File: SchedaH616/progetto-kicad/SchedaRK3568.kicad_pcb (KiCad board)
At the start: 6 copper layers, 50 x 70 mm, 443 parts, among them J1 BUS_POWER_MIKILAB, J103 DC-005-5A-2.0, J104 TYPE-C-31-M-12, J2 BUS_MIKILAB_MAIN, J301 UART2 debug, J401 DM3AT-SF-PEJM5, J501 HR911130C, J601 U.FL, J701 SMA antenna, J702 SMA PPS OUT, J703 SMA STROBE IN, J704 PPS/STROBE, J801 TYPE-C-31-M-12, SW301 RESET, SW302 RECOVERY, U101 TPS56637RPAR, U103 TPS2121RUXR, U104 FUSB302BMPX, U105 SY6280AAC, U107 TPD2EUSB30ADRTR, U108 TPS2121RUXR, U201 RK809-5, U202 TCS4525_WT, U203 TPS563201DDCR, U204 AP2112K-1.8TRG1, U205 AP2112K-2.5TRG1, U301 RK3568, U302 TPD4E05U06DQA, U303 TPD4E05U06DQA, U304 TPD4E05U06DQA, U305 TPD4E05U06DQA, U306 TPD4E05U06DQA, U307 TPD4E05U06DQA, U401 K4AAG165WA-BCWE, U402 FEMDNN064G-C9A61, U403 TPD4E05U06DQA, U404 TPD4E05U06DQA, U501 RTL8211F-CG, U502 25AA02E48T-I/OT, U601 AP6256, U701 NEO-M9N-00B, U702 74LVC1G17, U703 74LVC1G17, U801 TPS2553DBVR, U802 USBLC6-2SC6, Y201 32.768kHz, Y301 24MHz, Y501 25MHz

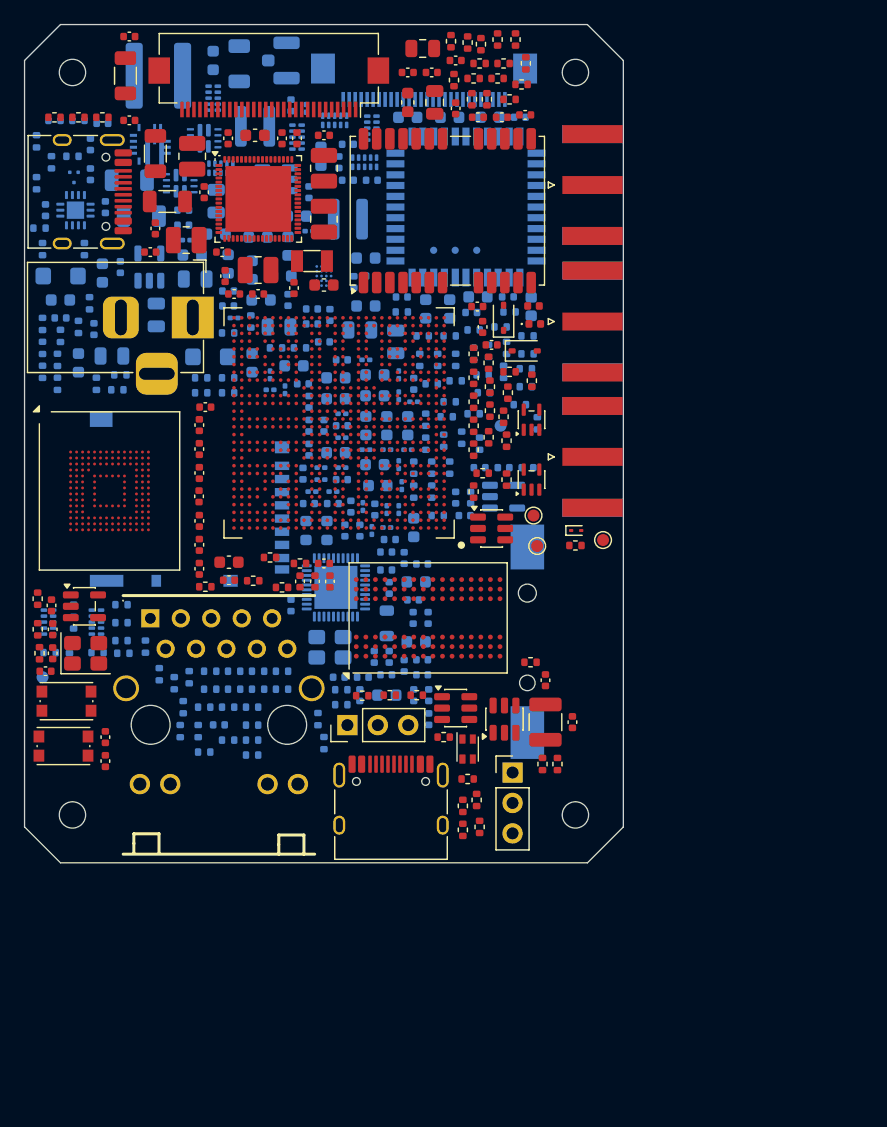
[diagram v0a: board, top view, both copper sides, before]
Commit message: SchedaH616: componenti specifici dalla libreria MIKILAB
- simbolo e footprint MIKILAB per RK809-5, TCS4525, K4AAG165WA-BCWE, FEMDNN064G-C9A61,
  AP2112K-1.8TRG1, TPS56637RPAR, TPS2121RUXR, SY6280AAC, TPS563201DDCR, TPS2553DBVR,
  TYPE-C-31-M-12, FH12-30S-0.5SH, FPC-05F-28PH20, HR911130C, 25AA02E48T-I/OT, DM3AT-SF-PEJM5;
  simbolo MIKILAB per l'AP6256
- restano nella libreria di progetto: RK3568 (pad EasyEDA da 0.35 mm, niente fanout 5/5 mil),
  simbolo RTL8211F (quello MIKILAB ha pin di alimentazione nascosti), footprint AP6256 LGA-47,
  portapila BS-12; motivazioni in docs/scelte-progetto.md
- kilib.mik() carica simboli e footprint dalla libreria (variabile MIKILAB); matrice ERC:
  pin unspecified dei simboli EasyEDA OK
- netlist identica a 4ca35fc (439 componenti, 314 net); ERC 0, parita' 0, DRC 0 (solo
  collegamenti da fare); footprint corretti nella libreria MIKILAB 8b990c4

Co-Authored-By: Claude Opus 5.5 (1M context) <noreply@anthropic.com>
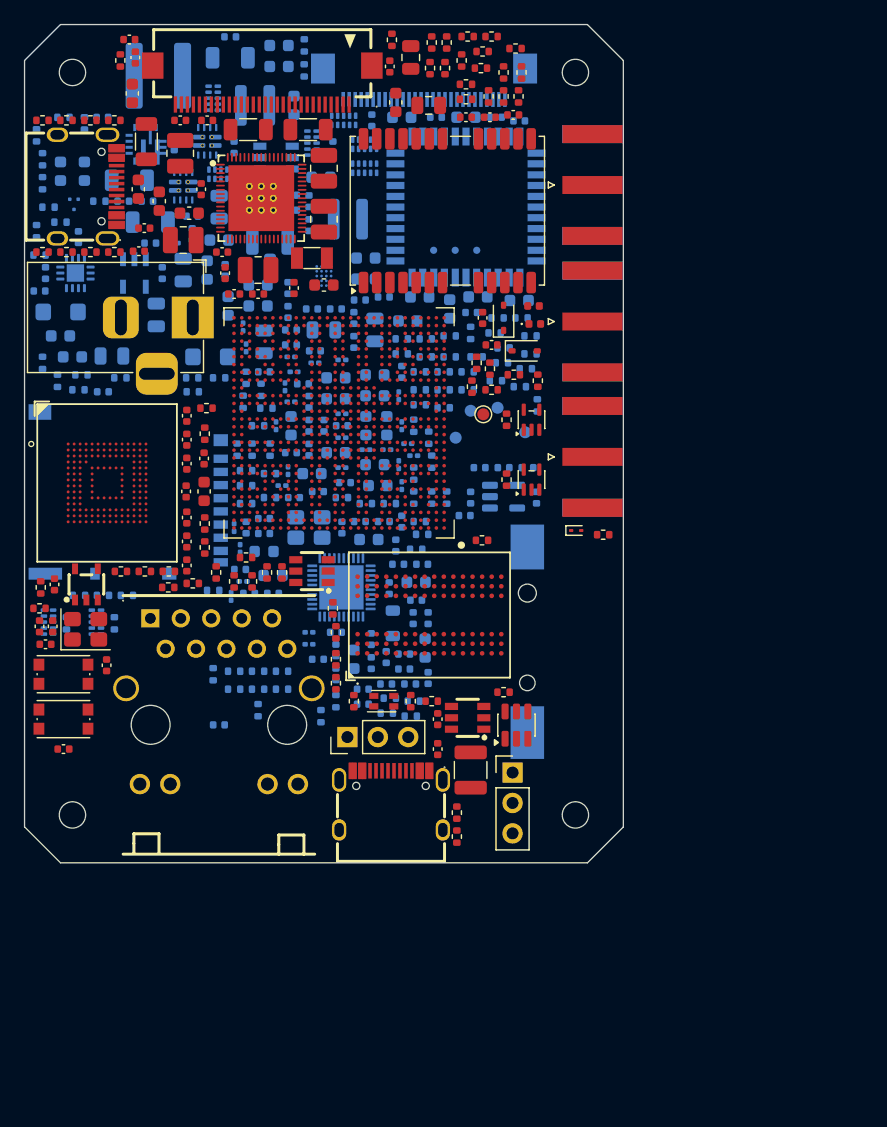
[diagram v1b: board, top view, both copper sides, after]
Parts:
- C104, C133, C203, C208, C210, C217, C228, C260, C339, C341, C425, C511, C512, C513, C515, C607, C702, R315, R319, R329, R331, R339, R402, R418, R420, R421, R516, R601, R603, R604, R609, R806, R807, TP202, TP702: moved to B.Cu
- C127, C134, C206, C209, C212, C213, C220, C233, C239, R107, R108, R110, R111, R114, R115, R202, R203, R309, R333, R336, R407, R409, R410, R412, R503, R507, R509, R511, R519, R526, R602, R605, R608: moved to F.Cu
- J1: footprint Connector_FFC-FPC:Hirose_FH12-30S-0.5SH_1x30-1MP_P0.50mm_Horizontal -> MIKILAB_FH12_30S_0_5SH:FPC-SMD_FH12-30S-0.5SH-55
- J104, J801: footprint Connector_USB:USB_C_Receptacle_HRO_TYPE-C-31-M-12 -> MIKILAB_TYPE_C_31_M_12:USB-C_SMD-TYPE-C-31-M-12_1
- J2: footprint Scheda:FPC-05F-28PH20 -> MIKILAB_FPC_05F_28PH20:FPC-SMD_28P-P0.50_FPC-05F-28PH20
- J401: footprint Connector_Card:microSD_HC_Hirose_DM3AT-SF-PEJM5 -> MIKILAB_DM3AT_SF_PEJM5:SD-SMD_DM3AT-SF-PEJM5
- J501: footprint Scheda:RJ45-TH_HR911130C -> MIKILAB_HR911130C:RJ45-TH_HR911130C
- U101: footprint Scheda:Texas_RPA0010A_VQFN-HR-10_3x3mm -> MIKILAB_TPS56637RPAR:VQFN-HR-10_L3.0-W3.0_RPA
- U103, U108: footprint Package_DFN_QFN:Texas_VQFN-HR-12_2x2.5mm_P0.5mm -> MIKILAB_TPS2121RUXR:IC_TPS2121RUXR
- U105: footprint Package_TO_SOT_SMD:SOT-23-5 -> MIKILAB_SY6280AAC:SOT-23-5_L3.0-W1.7-P0.95-LS2.8-BL
- U201: footprint Package_DFN_QFN:ArtInChip_QFN-68-1EP_7x7mm_P0.35mm_EP5.49x5.49mm -> MIKILAB_RK809_5:QFN-68_L7.0-W7.0-P0.35-BL-EP5.5
- U202: footprint Package_CSP:DiodesInc_GEA20_WLCSP-20_1.7x2.1mm_Layout4x5_P0.4mm -> MIKILAB_TCS4525:TCS4525_WLCSP-20_1.6x2.0mm_P0.4mm
- U203: footprint Package_TO_SOT_SMD:SOT-23-6 -> MIKILAB_TPS563201DDCR:TPS563201DDCR_SOT-23-6_L2.9-W1.6-P0.95-LS2.8-BR
- U204: footprint Package_TO_SOT_SMD:SOT-23-5 -> MIKILAB_AP2112K_1_8TRG1:SOT-25_L3.0-W1.6-P0.95-LS2.8-BL
- U401: footprint Package_BGA:BGA-96_9.0x13.0mm_Layout2x3x16_P0.8mm -> MIKILAB_K4AAG165WA_BCWE:BGA-96_L13.3-W10.3-P0.80_K4AAG165WA-BCWE
- U402: footprint Package_BGA:LFBGA-153_11.5x13mm_Layout14x14_P0.5mm -> MIKILAB_FEMDNN064G_C9A61:BGA-153_L13.0-W11.5-P0.50-TL_FORESEE_FEMDME
- U501: footprint Package_DFN_QFN:QFN-40-1EP_5x5mm_P0.4mm_EP3.6x3.6mm -> MIKILAB_RTL8211F_CG:QFN40P500X500X90-41N
- U502: footprint Package_TO_SOT_SMD:SOT-23-6 -> MIKILAB_25AA02E48T_I_OT:SOT-23-6_L2.9-W1.6-P0.95-LS2.8-BR
- U801: footprint Package_TO_SOT_SMD:SOT-23-6 -> MIKILAB_TPS2553DBVR:TPS2553DBVR_SOT-23-6_L2.9-W1.6-P0.95-LS2.8-BR
- moved TP101 42.1 mm to (137.3, 132.3)
- moved R203 34.5 mm to (135.2, 101.5), turned to 90 degrees
- moved R121 33.9 mm to (101.0, 109.2), turned to 90 degrees
- moved R115 33.5 mm to (130.7, 101.3)
- moved R122 33.4 mm to (101.0, 117.2), turned to 90 degrees
- moved R317 33.4 mm to (104.5, 130.5)
- moved R202 32.8 mm to (134.0, 101.5), turned to 90 degrees
- moved R604 32.4 mm to (123.4, 101.7)
- moved R128 32.0 mm to (133.5, 127.8), turned to 0 degrees
- moved C607 30.5 mm to (120.0, 129.0)
- moved R527 29.4 mm to (135.2, 139.5), turned to 90 degrees
- moved R313 27.5 mm to (108.0, 129.5), turned to 0 degrees
- moved R521 27.2 mm to (116.0, 145.8), turned to 90 degrees
- moved R516 25.9 mm to (117.5, 155.5), turned to 0 degrees
- moved C339 25.6 mm to (122.2, 126.8)
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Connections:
- U402 pad A1: (no net) -> unconnected-(U402B-NC-PadA1)
- U402 pad A10: (no net) -> unconnected-(U402B-NC-PadA10)
- U402 pad A11: (no net) -> unconnected-(U402B-NC-PadA11)
- U402 pad A12: (no net) -> unconnected-(U402B-NC-PadA12)
- U402 pad A13: (no net) -> unconnected-(U402B-NC-PadA13)
- U402 pad A14: (no net) -> unconnected-(U402B-NC-PadA14)
- U402 pad A2: (no net) -> unconnected-(U402B-NC-PadA2)
- U402 pad A7: (no net) -> unconnected-(U402A-RFU-PadA7)
- U402 pad A8: (no net) -> unconnected-(U402B-NC-PadA8)
- U402 pad A9: (no net) -> unconnected-(U402B-NC-PadA9)
- U402 pad B1: (no net) -> unconnected-(U402B-NC-PadB1)
- U402 pad B10: (no net) -> unconnected-(U402B-NC-PadB10)
- U402 pad B11: (no net) -> unconnected-(U402B-NC-PadB11)
- U402 pad B12: (no net) -> unconnected-(U402B-NC-PadB12)
- U402 pad B13: (no net) -> unconnected-(U402B-NC-PadB13)
- U402 pad B14: (no net) -> unconnected-(U402B-NC-PadB14)
- U402 pad B7: (no net) -> unconnected-(U402B-NC-PadB7)
- U402 pad B8: (no net) -> unconnected-(U402B-NC-PadB8)
- U402 pad B9: (no net) -> unconnected-(U402B-NC-PadB9)
- U402 pad C1: (no net) -> unconnected-(U402B-NC-PadC1)
- U402 pad C10: (no net) -> unconnected-(U402B-NC-PadC10)
- U402 pad C11: (no net) -> unconnected-(U402B-NC-PadC11)
- U402 pad C12: (no net) -> unconnected-(U402B-NC-PadC12)
- U402 pad C13: (no net) -> unconnected-(U402B-NC-PadC13)
- U402 pad C14: (no net) -> unconnected-(U402B-NC-PadC14)
- U402 pad C3: (no net) -> unconnected-(U402B-NC-PadC3)
- U402 pad C5: (no net) -> unconnected-(U402B-NC-PadC5)
- U402 pad C7: (no net) -> unconnected-(U402B-NC-PadC7)
- U402 pad C8: (no net) -> unconnected-(U402B-NC-PadC8)
- U402 pad C9: (no net) -> unconnected-(U402B-NC-PadC9)
- U402 pad D1: (no net) -> unconnected-(U402B-NC-PadD1)
- U402 pad D12: (no net) -> unconnected-(U402B-NC-PadD12)
- U402 pad D13: (no net) -> unconnected-(U402B-NC-PadD13)
- U402 pad D14: (no net) -> unconnected-(U402B-NC-PadD14)
- U402 pad D2: (no net) -> unconnected-(U402B-NC-PadD2)
- U402 pad D3: (no net) -> unconnected-(U402B-NC-PadD3)
- U402 pad D4: (no net) -> unconnected-(U402B-NC-PadD4)
- U402 pad E1: (no net) -> unconnected-(U402B-NC-PadE1)
- U402 pad E10: (no net) -> unconnected-(U402A-VSF-PadE10)
- U402 pad E12: (no net) -> unconnected-(U402B-NC-PadE12)
- U402 pad E13: (no net) -> unconnected-(U402B-NC-PadE13)
- U402 pad E14: (no net) -> unconnected-(U402B-NC-PadE14)
- U402 pad E2: (no net) -> unconnected-(U402B-NC-PadE2)
- U402 pad E3: (no net) -> unconnected-(U402B-NC-PadE3)
- U402 pad E5: (no net) -> unconnected-(U402A-RFU-PadE5)
- U402 pad E8: (no net) -> unconnected-(U402A-VSF-PadE8)
- U402 pad E9: (no net) -> unconnected-(U402A-VSF-PadE9)
- U402 pad F1: (no net) -> unconnected-(U402B-NC-PadF1)
- U402 pad F10: (no net) -> unconnected-(U402A-VSF-PadF10)
- U402 pad F12: (no net) -> unconnected-(U402B-NC-PadF12)
- U402 pad F13: (no net) -> unconnected-(U402B-NC-PadF13)
- U402 pad F14: (no net) -> unconnected-(U402B-NC-PadF14)
- U402 pad F2: (no net) -> unconnected-(U402B-NC-PadF2)
- U402 pad F3: (no net) -> unconnected-(U402B-NC-PadF3)
- U402 pad G1: (no net) -> unconnected-(U402B-NC-PadG1)
- U402 pad G10: (no net) -> unconnected-(U402A-VSF-PadG10)
- U402 pad G12: (no net) -> unconnected-(U402B-NC-PadG12)
- U402 pad G13: (no net) -> unconnected-(U402B-NC-PadG13)
- U402 pad G14: (no net) -> unconnected-(U402B-NC-PadG14)
- U402 pad G2: (no net) -> unconnected-(U402B-NC-PadG2)
- U402 pad G3: (no net) -> unconnected-(U402A-RFU-PadG3)
- U402 pad H1: (no net) -> unconnected-(U402B-NC-PadH1)
- U402 pad H12: (no net) -> unconnected-(U402B-NC-PadH12)
- U402 pad H13: (no net) -> unconnected-(U402B-NC-PadH13)
- U402 pad H14: (no net) -> unconnected-(U402B-NC-PadH14)
- U402 pad H2: (no net) -> unconnected-(U402B-NC-PadH2)
- U402 pad H3: (no net) -> unconnected-(U402B-NC-PadH3)
- U402 pad J1: (no net) -> unconnected-(U402B-NC-PadJ1)
- U402 pad J12: (no net) -> unconnected-(U402B-NC-PadJ12)
- U402 pad J13: (no net) -> unconnected-(U402B-NC-PadJ13)
- U402 pad J14: (no net) -> unconnected-(U402B-NC-PadJ14)
- U402 pad J2: (no net) -> unconnected-(U402B-NC-PadJ2)
- U402 pad J3: (no net) -> unconnected-(U402B-NC-PadJ3)
- U402 pad K1: (no net) -> unconnected-(U402B-NC-PadK1)
- U402 pad K10: (no net) -> unconnected-(U402A-VSF-PadK10)
- U402 pad K12: (no net) -> unconnected-(U402B-NC-PadK12)
- U402 pad K13: (no net) -> unconnected-(U402B-NC-PadK13)
- U402 pad K14: (no net) -> unconnected-(U402B-NC-PadK14)
- U402 pad K2: (no net) -> unconnected-(U402B-NC-PadK2)
- U402 pad K3: (no net) -> unconnected-(U402B-NC-PadK3)
- U402 pad K6: (no net) -> unconnected-(U402A-RFU-PadK6)
- U402 pad K7: (no net) -> unconnected-(U402A-RFU-PadK7)
- U402 pad L1: (no net) -> unconnected-(U402B-NC-PadL1)
- U402 pad L12: (no net) -> unconnected-(U402B-NC-PadL12)
- U402 pad L13: (no net) -> unconnected-(U402B-NC-PadL13)
- U402 pad L14: (no net) -> unconnected-(U402B-NC-PadL14)
- U402 pad L2: (no net) -> unconnected-(U402B-NC-PadL2)
- U402 pad L3: (no net) -> unconnected-(U402B-NC-PadL3)
- U402 pad M1: (no net) -> unconnected-(U402B-NC-PadM1)
- U402 pad M10: (no net) -> unconnected-(U402B-NC-PadM10)
- U402 pad M11: (no net) -> unconnected-(U402B-NC-PadM11)
- U402 pad M12: (no net) -> unconnected-(U402B-NC-PadM12)
- U402 pad M13: (no net) -> unconnected-(U402B-NC-PadM13)
- U402 pad M14: (no net) -> unconnected-(U402B-NC-PadM14)
- U402 pad M2: (no net) -> unconnected-(U402B-NC-PadM2)
- U402 pad M3: (no net) -> unconnected-(U402B-NC-PadM3)
- U402 pad M7: (no net) -> unconnected-(U402B-NC-PadM7)
- U402 pad M8: (no net) -> unconnected-(U402B-NC-PadM8)
- U402 pad M9: (no net) -> unconnected-(U402B-NC-PadM9)
- U402 pad N1: (no net) -> unconnected-(U402B-NC-PadN1)
- U402 pad N10: (no net) -> unconnected-(U402B-NC-PadN10)
- U402 pad N11: (no net) -> unconnected-(U402B-NC-PadN11)
- U402 pad N12: (no net) -> unconnected-(U402B-NC-PadN12)
- U402 pad N13: (no net) -> unconnected-(U402B-NC-PadN13)
- U402 pad N14: (no net) -> unconnected-(U402B-NC-PadN14)
- U402 pad N3: (no net) -> unconnected-(U402B-NC-PadN3)
- U402 pad N6: (no net) -> unconnected-(U402B-NC-PadN6)
- U402 pad N7: (no net) -> unconnected-(U402B-NC-PadN7)
- U402 pad N8: (no net) -> unconnected-(U402B-NC-PadN8)
- U402 pad N9: (no net) -> unconnected-(U402B-NC-PadN9)
- U402 pad P1: (no net) -> unconnected-(U402B-NC-PadP1)
- U402 pad P10: (no net) -> unconnected-(U402B-NC-PadP10)
- U402 pad P11: (no net) -> unconnected-(U402B-NC-PadP11)
- U402 pad P12: (no net) -> unconnected-(U402B-NC-PadP12)
- U402 pad P13: (no net) -> unconnected-(U402B-NC-PadP13)
- U402 pad P14: (no net) -> unconnected-(U402B-NC-PadP14)
- U402 pad P2: (no net) -> unconnected-(U402B-NC-PadP2)
- U402 pad P7: (no net) -> unconnected-(U402B-NC-PadP7)
- U402 pad P8: (no net) -> unconnected-(U402B-NC-PadP8)
- U402 pad P9: (no net) -> unconnected-(U402B-NC-PadP9)

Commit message: SchedaH616: placement RK3568 su 70 x 90 mm, componenti sul top
- scheda 70 x 90 mm, angoli 3 mm, 4 fori 2.2 mm; 6 strati, 5 mil, via-in-pad 0.25/0.15
- RK3568 al centro, DDR4 sotto l'angolo DDR; J1 e J2 entrambi sul top
- 388 componenti sul top, 51 sul bottom (solo disaccoppiamento sotto RK3568 e DDR4)
- schema invariato: ERC 0, parita' 0, DRC 0 (solo collegamenti da fare)

Co-Authored-By: Claude Opus 5.5 (1M context) <noreply@anthropic.com>
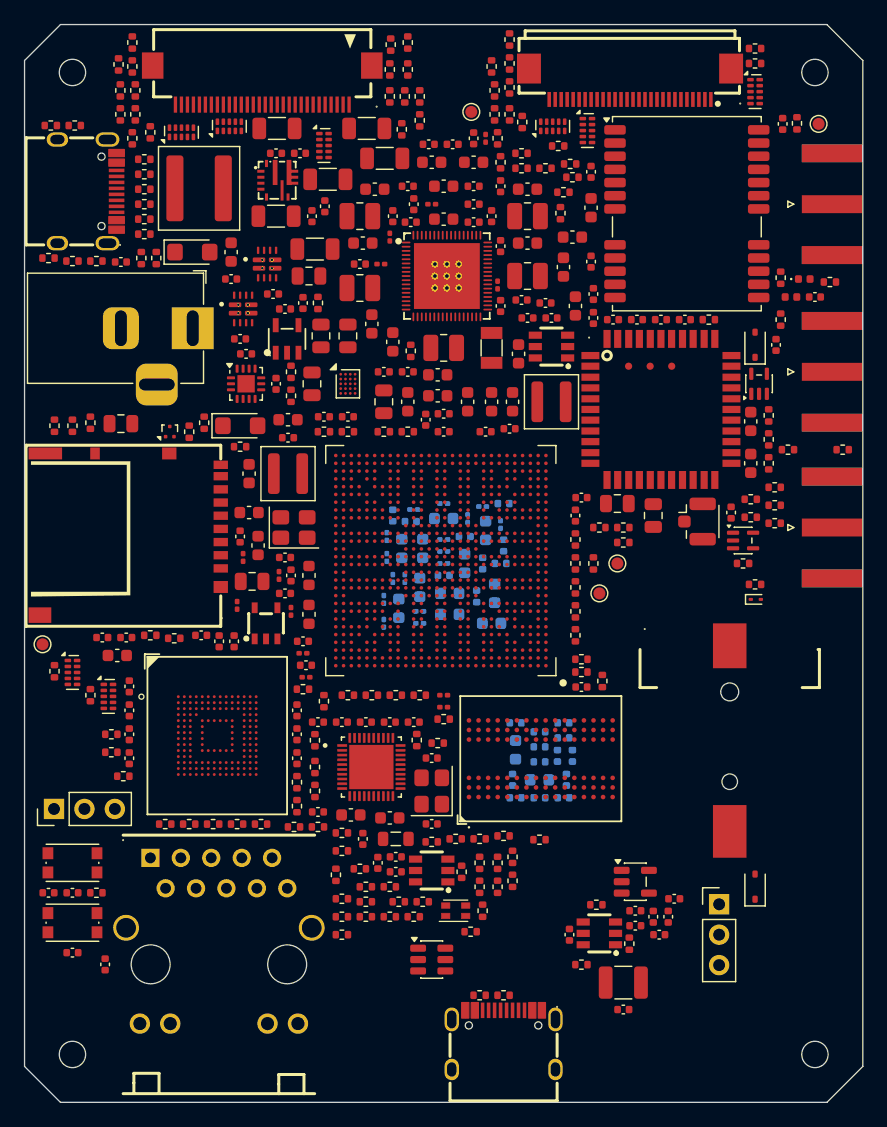
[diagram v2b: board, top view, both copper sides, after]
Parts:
- BT701, C101, C102, C103, C104, C106, C107, C108, C109, C110, C111, C112, C113, C114, C115, C125, C126, C132, C133, C135, C136, C201, C202, C203, C204, C205, C208, C210, C211, C216, C217, C219, C221, C222, C223, C224, C226, C227, C228, C229, C231, C235, C236, C237, C240, C241, C243, C244, C245, C246, C247, C248, C249, C250, C251, C252, C253, C254, C260, C261, C262, C263, C264, C305, C306, C307, C308, C328, C329, C330, C331, C338, C339, C340, C341, C342, C343, C344, C345, C346, C347, C348, C353, C362, C363, C403, C417, C418, C425, C501, C502, C503, C504, C505, C506, C507, C508, C509, C510, C511, C512, C513, C514, C515, C601, C603, C605, C606, C607, C701, C702, C706, D101, D102, FB301, FB302, J2, J401, J601, L101, L206, L207, L501, R101, R102, R103, R104, R112, R113, R116, R121, R122, R123, R124, R125, R126, R127, R128, R129, R130, R201, R204, R205, R206, R207, R211, R212, R213, R214, R302, R303, R304, R305, R306, R307, R308, R310, R311, R313, R315, R316, R317, R318, R319, R328, R329, R330, R331, R334, R335, R337, R338, R339, R4, R402, R403, R404, R408, R413, R414, R415, R416, R417, R418, R419, R420, R421, R422, R504, R505, R506, R508, R510, R512, R513, R514, R515, R516, R517, R518, R520, R522, R523, R524, R525, R527, R528, R529, R601, R603, R604, R606, R609, R704, R806, R807, TP101, TP201, TP202, TP702, U101, U103, U104, U105, U107, U108, U202, U203, U205, U302, U303, U304, U305, U306, U307, U403, U404, U501, U601, Y501: moved to F.Cu
- moved C258 54.5 mm to (146.0, 141.0), turned to 90 degrees
- moved C239 52.3 mm to (146.5, 139.5), turned to 0 degrees
- moved R604 52.2 mm to (162.1, 136.6)
- moved D704 48.7 mm to (161.0, 172.0), turned to 90 degrees
- moved J601 43.0 mm to (156.6, 141.5), turned to 0 degrees
- moved R216 43.0 mm to (150.0, 142.0)
- moved R217 42.7 mm to (150.0, 143.2)
- moved C256 41.1 mm to (149.5, 140.0), turned to 0 degrees
- moved C607 40.7 mm to (159.0, 140.8), turned to 90 degrees
- moved TP101 40.7 mm to (101.5, 151.8)
- moved R215 40.7 mm to (148.0, 142.0), turned to 0 degrees
- moved C262 40.4 mm to (151.0, 175.2)
- moved R524 40.0 mm to (126.5, 174.5), turned to 0 degrees
- moved R523 39.1 mm to (130.5, 174.5)
- moved C257 39.0 mm to (152.5, 141.0), turned to 90 degrees
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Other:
- board size 50 x 70 mm -> 70 x 90 mm

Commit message: SchedaH616: passivi 0603, microSD sul bottom, USB-C affiancate
- passivi 0603 di default; 0201/0402 solo per il disaccoppiamento sotto RK3568 e DDR4,
  le serie RGMII/clock/USB, DDR_RZQ, ZQ e VREF della DDR4
  (C: 29x0201, 31x0402, 133x0603; R: 24x0402, 133x0603)
- microSD J401 sul bottom, apertura sul bordo sinistro
- USB-C host J801 e OTG/alimentazione J104 affiancate sul bordo basso, con ESD,
  TPS2553, TPS2121, FUSB302B e SY6280 accanto
- 387 componenti sul top, 52 sul bottom; ERC 0, parita' 0, DRC 0 (solo collegamenti)

Co-Authored-By: Claude Opus 5.5 (1M context) <noreply@anthropic.com>
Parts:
- C103, C108, C109, C110, C111, C112, C114, C125, C126, C132, C133, C134, C136, C205, C206, C207, C208, C210, C214, C217, C222, C225, C226, C227, C228, C229, C230, C231, C232, C233, C234, C236, C237, C238, C239, C240, C241, C242, C243, C244, C247, C248, C254, C255, C258, C259, C260, C261, C262, C263, C264, C301, C302, C303, C304, C401, C419, C420, C421, C422, C423, C424, C425, C427, C501, C502, C503, C505, C506, C507, C508, C510, C511, C512, C513, C514, C515, C602, C604, C605, C606, C607, C702, C703, C704, C705, C706, C801, C803: footprint Capacitor_SMD:C_0402_1005Metric -> Capacitor_SMD:C_0603_1608Metric
- J401: moved to B.Cu
- R1, R101, R102, R103, R104, R105, R106, R107, R108, R109, R110, R111, R112, R113, R114, R115, R116, R121, R122, R123, R124, R125, R126, R127, R128, R129, R130, R2, R201, R202, R203, R204, R205, R206, R207, R208, R209, R210, R211, R212, R213, R214, R215, R216, R217, R3, R301, R302, R303, R304, R305, R306, R307, R308, R309, R310, R311, R312, R313, R317, R318, R319, R320, R321, R322, R323, R324, R325, R326, R327, R328, R329, R330, R331, R332, R333, R334, R335, R336, R337, R338, R339, R4, R406, R407, R408, R409, R410, R411, R412, R413, R414, R415, R417, R418, R419, R420, R421, R422, R507, R508, R509, R510, R511, R512, R513, R514, R515, R516, R517, R518, R519, R520, R521, R522, R523, R601, R602, R603, R604, R605, R606, R607, R608, R702, R703, R704, R705, R706, R801, R802, R804, R805: footprint Resistor_SMD:R_0402_1005Metric -> Resistor_SMD:R_0603_1608Metric
- moved R315 92.6 mm to (153.0, 185.8), turned to 90 degrees
- moved R314 85.6 mm to (149.5, 181.1)
- moved J104 82.5 mm to (147.5, 184.8), turned to 0 degrees
- moved R111 81.6 mm to (156.5, 182.0), turned to 90 degrees
- moved R313 80.8 mm to (141.5, 183.5)
- moved D102 72.1 mm to (154.0, 179.0)
- moved C107 72.1 mm to (154.0, 181.0), turned to 0 degrees
- moved C112 71.6 mm to (154.0, 182.8)
- moved R109 71.4 mm to (143.5, 180.5)
- moved R108 71.1 mm to (159.2, 170.5), turned to 0 degrees
- moved R110 70.9 mm to (141.0, 180.0), turned to 90 degrees
- moved TP701 70.1 mm to (101.8, 135.8)
- moved R107 68.0 mm to (156.0, 170.5), turned to 0 degrees
- moved R112 64.1 mm to (159.0, 181.5), turned to 0 degrees
- moved R113 63.0 mm to (162.5, 179.5)
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
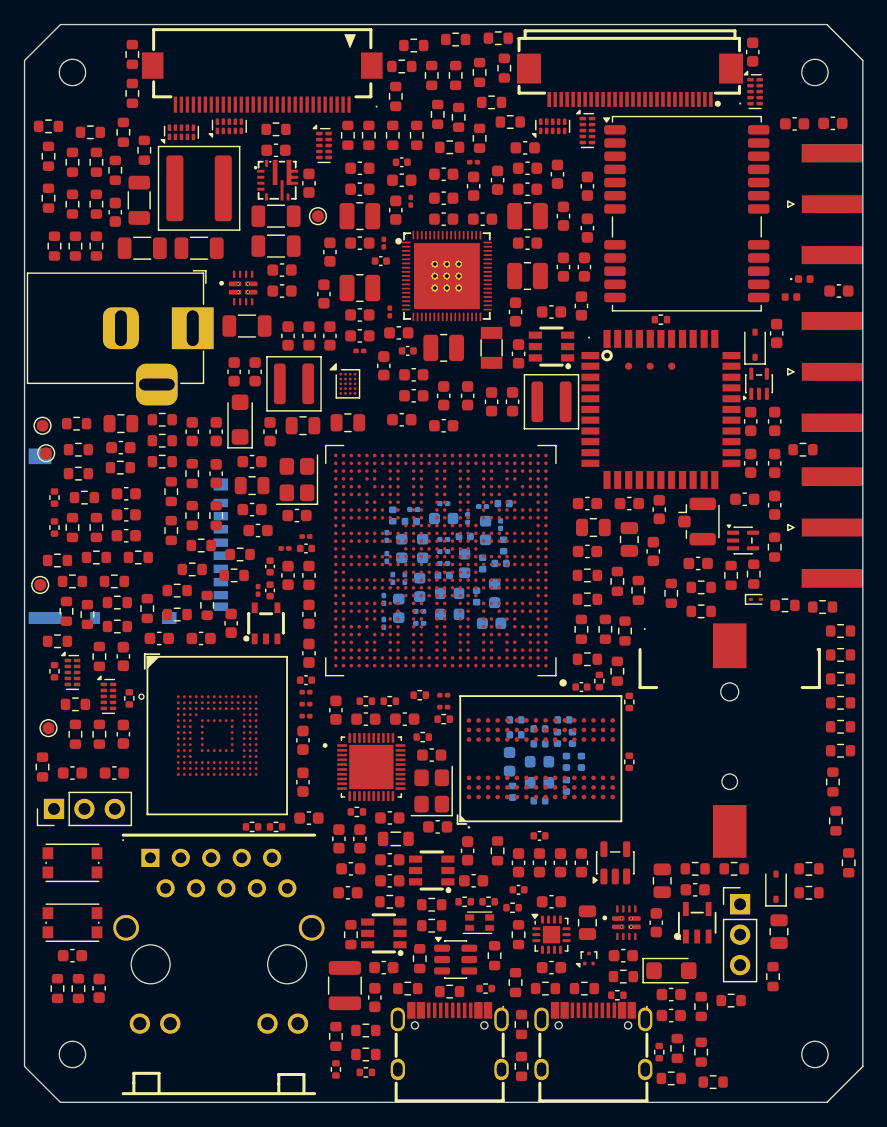
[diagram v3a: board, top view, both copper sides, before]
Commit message: SchedaH616: niente 0201, disaccoppiamento 0402 sotto le BGA
- i 29 condensatori 0201 del RK3568 diventano 0402 (stessi valori): minimo 0402 per i passivi
- disaccoppiamento di RK3568 (C305-C363) e DDR4 (C404-C418) sempre ancorato al suo package:
  59/59 sotto il RK3568 e 15/15 sotto la DDR4, sul bottom (prima 23 finivano sul top vicino alla PMIC)
- 364 componenti sul top, 75 sul bottom (74 condensatori + microSD); scheda sempre 70 x 90
- ERC 0, parita' 0, DRC 0 (solo collegamenti da fare)

Co-Authored-By: Claude Opus 5.5 (1M context) <noreply@anthropic.com>
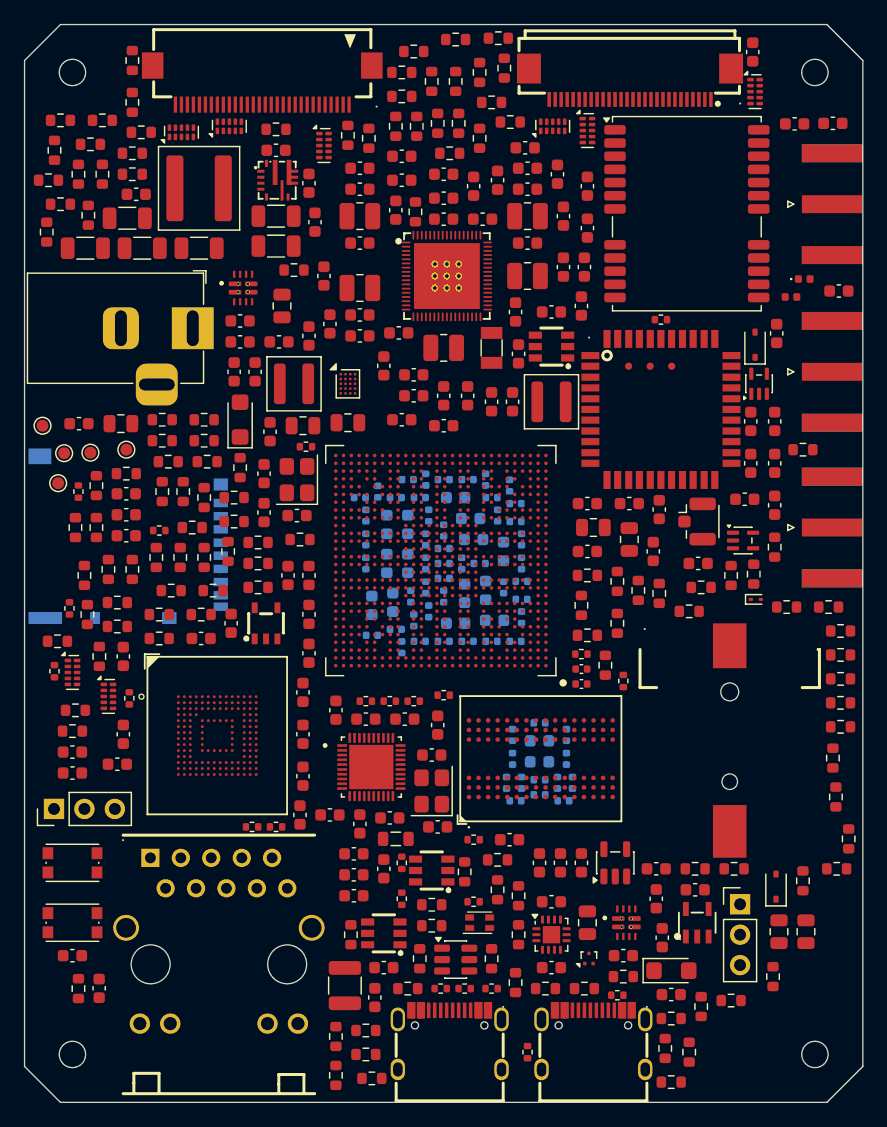
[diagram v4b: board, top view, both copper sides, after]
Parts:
- C305, C307, C329, C330, C331, C337, C339, C341, C343, C345, C417, C418: moved to B.Cu
- C306, C308, C328, C338, C340, C342, C344, C346, C347, C348, C353, C362, C363: footprint Capacitor_SMD:C_0201_0603Metric -> Capacitor_SMD:C_0402_1005Metric; moved to B.Cu
- C309, C310, C316, C323, C332, C333, C349, C350, C351, C354, C355, C356, C357, C358, C359, C360: footprint Capacitor_SMD:C_0201_0603Metric -> Capacitor_SMD:C_0402_1005Metric
- C401, C402: moved to F.Cu
- moved R529 54.1 mm to (104.5, 139.0), turned to 90 degrees
- moved R605 52.7 mm to (132.6, 115.6), turned to 90 degrees
- moved R420 49.9 mm to (114.0, 142.0)
- moved R419 48.1 mm to (155.5, 149.0)
- moved R509 43.2 mm to (111.0, 144.5), turned to 90 degrees
- moved R418 41.7 mm to (115.0, 144.5), turned to 90 degrees
- moved R417 39.1 mm to (153.0, 147.5), turned to 90 degrees
- moved R211 36.4 mm to (134.5, 108.2), turned to 90 degrees
- moved C342 36.4 mm to (129.0, 151.0), turned to 0 degrees
- moved R337 34.5 mm to (119.5, 147.0), turned to 0 degrees
- moved R520 31.5 mm to (104.5, 180.5)
- moved C353 30.8 mm to (128.5, 141.0), turned to 90 degrees
- moved TP101 28.9 mm to (101.5, 133.5)
- moved C341 27.6 mm to (129.5, 139.0), turned to 90 degrees
- moved R124 26.6 mm to (115.0, 134.8), turned to 0 degrees
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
